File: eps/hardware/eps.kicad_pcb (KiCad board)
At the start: 4 copper layers, 80 x 80 mm, 401 parts, among them J1 USB_C_Receptacle_USB2.0_16P, J10 Conn_02x20_Counter_Clockwise, J11 Conn_01x03, J12 Conn_01x03, J2 Conn_01x02, J3 Conn_01x02, J4 Conn_01x02, J5 Conn_01x02, J6 Conn_01x02, J7 Conn_01x02, J8 Conn_01x02, J9 Conn_02x03_Odd_Even, Q1 NMOS, Q10 IRLML0030, Q11 IRLML0030, Q12 IRLML0030, Q13 IRLML0030, Q14 IRLML0030, Q15 IRLML0030, Q16 IRLML0030, Q17 IRLML0030, Q18 IRLML0030, Q19 IRLML0030, Q2 NMOS, Q20 IRLML0030, Q3 NMOS, Q4 NMOS, Q5 IRLML0030, Q6 IRLML0030, Q7 IRLML0030, Q8 IRLML0030, Q9 IRLML0030, SW1 SW_Push, SW2 SW_SPDT, U1 TPS22810DRV, U10 STM32L496ZGTx, U11 NCS214RSQT2G, U12 74LVC1G07SE-7, U15 NCS214RSQT2G, U16 74LVC1G07SE-7, U19 NCS214RSQT2G, U2 LTC3130-1, U20 74LVC1G07SE-7, U23 NCS214RSQT2G, U24 74LVC1G07SE-7, U27 NCS214RSQT2G, U28 74LVC1G07SE-7, U3 LTC4162-L, U31 NCS214RSQT2G, U32 74LVC1G07SE-7, U35 NCS214RSQT2G, U36 74LVC1G07SE-7, U39 MP28167-A, U4 LTC4162-L, U40 MP28167-A, U41 LTC4415, U42 LTC4415, U5 NCS214RSQT2G, U6 74LVC1G07SE-7, U9 TPS35-Q1, Y1 8MHz, Y2 32KHz

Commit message: start placement
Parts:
- J5, L1, L2, L3, L4, L5, U5, U6, U7, U8: moved to B.Cu
- moved U3 196.0 mm to (232.2, 117.0), turned to 90 degrees
- moved U40 195.3 mm to (234.1, 80.2)
- moved U4 195.2 mm to (221.6, 57.8), turned to -90 degrees
- moved L5 193.3 mm to (234.1, 74.0), turned to 90 degrees
- moved J12 193.3 mm to (235.0, 59.5), turned to 180 degrees
- moved J11 185.4 mm to (230.5, 124.5)
- moved L3 183.7 mm to (224.5, 64.5), turned to -90 degrees
- moved J10 183.1 mm to (201.8, 57.4)
- moved L2 174.7 mm to (223.5, 117.0)
- moved J9 163.2 mm to (221.0, 74.5), turned to -90 degrees
- moved U10 161.0 mm to (203.3, 90.0)
- moved L4 153.4 mm to (236.5, 89.5), turned to 90 degrees
- moved U39 152.8 mm to (234.8, 97.3)
- moved J4 141.3 mm to (236.9, 105.5), turned to 90 degrees
- moved Y2 134.0 mm to (186.0, 84.5), turned to 90 degrees
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
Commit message: schematic fixes
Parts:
- removed J9: Conn_02x03_Odd_Even, Connector_PinHeader_2.54mm:PinHeader_2x03_P2.54mm_Vertical
- added J13: Conn_ARM_JTAG_SWD_10, Connector_PinHeader_1.27mm:PinHeader_2x05_P1.27mm_Vertical_SMD, F.Cu at (218.6, 75.0)
- C1, C10, C100, C101, C102, C103, C104, C105, C106, C107, C108, C11, C110, C111, C112, C113, C114, C115, C116, C117, C118, C119, C12, C120, C122, C123, C124, C125, C126, C127, C128, C129, C13, C130, C131, C132, C133, C134, C135, C136, C137, C138, C139, C14, C140, C141, C142, C143, C144, C15, C16, C17, C18, C19, C2, C20, C21, C22, C23, C24, C25, C26, C27, C28, C29, C3, C30, C31, C32, C33, C34, C35, C36, C37, C38, C39, C4, C40, C41, C42, C43, C44, C45, C46, C47, C49, C5, C51, C52, C53, C54, C55, C56, C57, C58, C59, C6, C60, C61, C62, C63, C64, C65, C66, C67, C68, C69, C7, C70, C71, C72, C73, C74, C75, C76, C77, C78, C79, C8, C80, C81, C82, C83, C84, C85, C86, C87, C88, C89, C9, C90, C91, C92, C93, C94, C95, C96, C97, C98, C99: footprint Capacitor_SMD:C_0603_1608Metric -> Capacitor_SMD:C_0402_1005Metric
- R1, R10, R100, R101, R102, R103, R104, R105, R106, R107, R108, R109, R11, R110, R111, R112, R113, R114, R115, R116, R117, R118, R119, R12, R120, R121, R122, R123, R124, R125, R126, R127, R128, R129, R13, R130, R131, R132, R133, R134, R135, R136, R137, R138, R139, R14, R140, R141, R142, R143, R144, R145, R146, R15, R16, R17, R18, R19, R2, R20, R21, R22, R23, R24, R25, R26, R27, R28, R29, R3, R30, R31, R32, R33, R34, R35, R36, R37, R38, R39, R4, R40, R41, R42, R43, R44, R45, R46, R47, R48, R49, R5, R50, R51, R52, R53, R54, R55, R56, R57, R58, R59, R6, R60, R61, R62, R63, R64, R65, R66, R67, R68, R69, R7, R70, R71, R72, R73, R74, R75, R76, R77, R78, R79, R8, R80, R81, R82, R83, R84, R85, R86, R87, R88, R89, R9, R90, R91, R92, R93, R94, R95, R96, R97, R98, R99: footprint Resistor_SMD:R_0603_1608Metric -> Resistor_SMD:R_0402_1005Metric
- U14, U18, U22, U26, U30, U34, U38: value ~ -> TPS22810DRVT
- U5, U6, U7: moved to F.Cu
- U8: value ~ -> TPS22810DRVT; moved to F.Cu
- moved U7 68.8 mm to (137.9, 120.1)
- moved U5 68.3 mm to (138.4, 124.3)
- moved U8 68.2 mm to (138.4, 112.7), turned to 0 degrees
- moved U6 68.1 mm to (138.5, 116.0)
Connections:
- C13 pad 2: Net-(U3-SW) -> Net-(C13-Pad2)
- C19 pad 2: Net-(U4-SW) -> Net-(C19-Pad2)
- J10 pad 01: (no net) -> GND
- J10 pad 02: (no net) -> /Current Monitors/RAIL_1_VOUT
- J10 pad 03: (no net) -> /Current Monitors/RAIL_2_VOUT
- J10 pad 04: (no net) -> /Current Monitors/RAIL_3_VOUT
- J10 pad 05: (no net) -> /Current Monitors/RAIL_4_VOUT
- J10 pad 06: (no net) -> /Current Monitors/RAIL_5_VOUT
- J10 pad 07: (no net) -> /Current Monitors/RAIL_6_VOUT
- J10 pad 08: (no net) -> /Current Monitors/RAIL_7_VOUT
- J10 pad 09: (no net) -> /Current Monitors/RAIL_8_VOUT
- L2 pad 1: Net-(U3-SW) -> Net-(C13-Pad2)
- L3 pad 1: Net-(U4-SW) -> Net-(C19-Pad2)
- U14 pad 7: (no net) -> unconnected-(U14-GND-Pad7)
- U18 pad 7: (no net) -> unconnected-(U18-GND-Pad7)
- U22 pad 7: (no net) -> unconnected-(U22-GND-Pad7)
- U26 pad 7: (no net) -> unconnected-(U26-GND-Pad7)
- U3 pad 25: Net-(U3-SW) -> Net-(C13-Pad2)
- U3 pad 26: (no net) -> Net-(C13-Pad2)
- U30 pad 7: (no net) -> unconnected-(U30-GND-Pad7)
- U34 pad 7: (no net) -> unconnected-(U34-GND-Pad7)
- U38 pad 7: (no net) -> unconnected-(U38-GND-Pad7)
- U4 pad 25: Net-(U4-SW) -> Net-(C19-Pad2)
- U4 pad 26: (no net) -> Net-(C19-Pad2)
- U8 pad 7: (no net) -> unconnected-(U8-GND-Pad7)

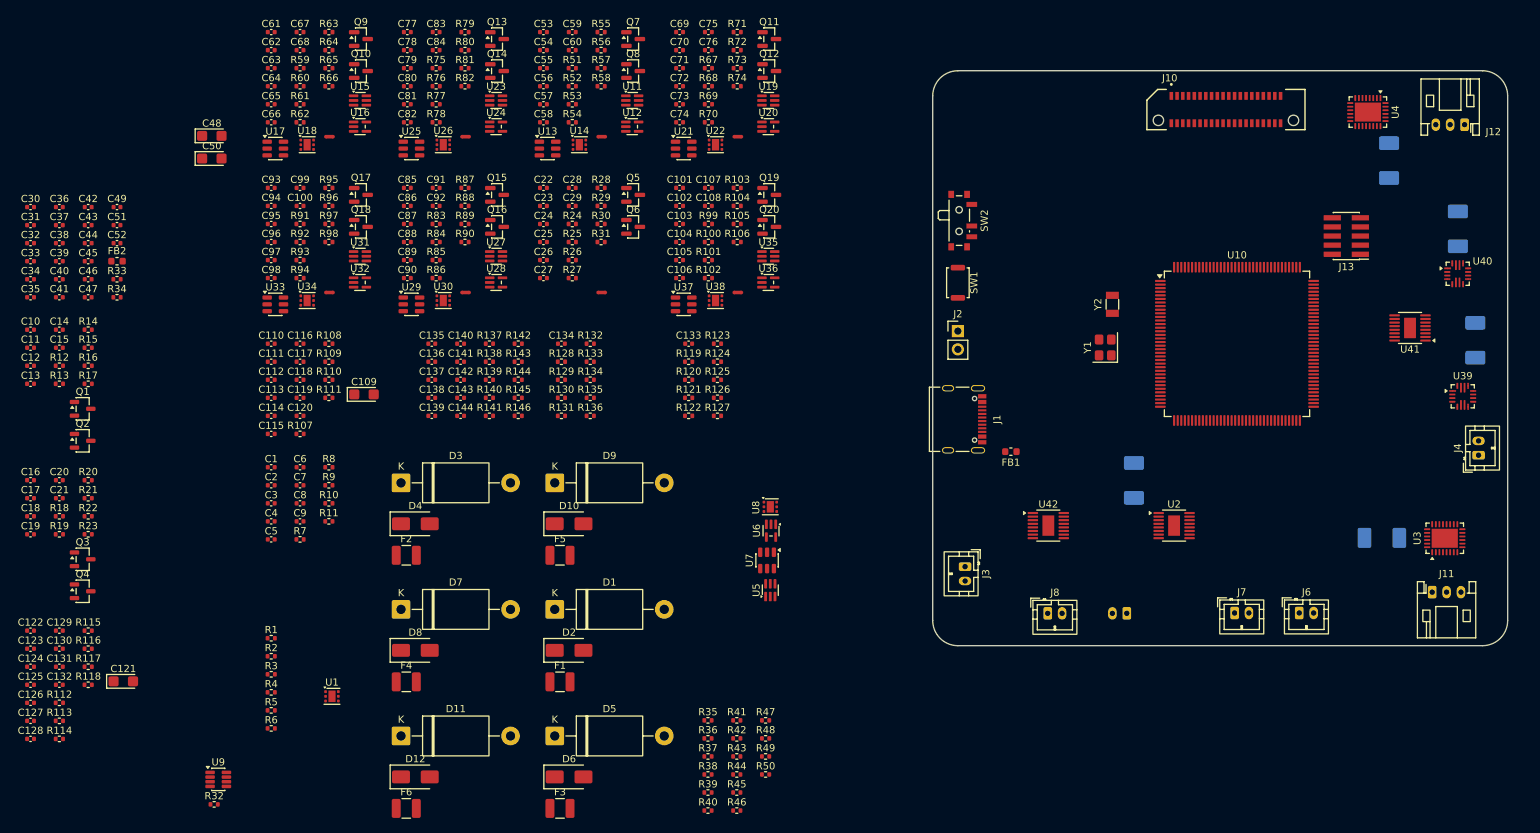
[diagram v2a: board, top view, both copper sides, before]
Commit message: fix all obvious schematic issues
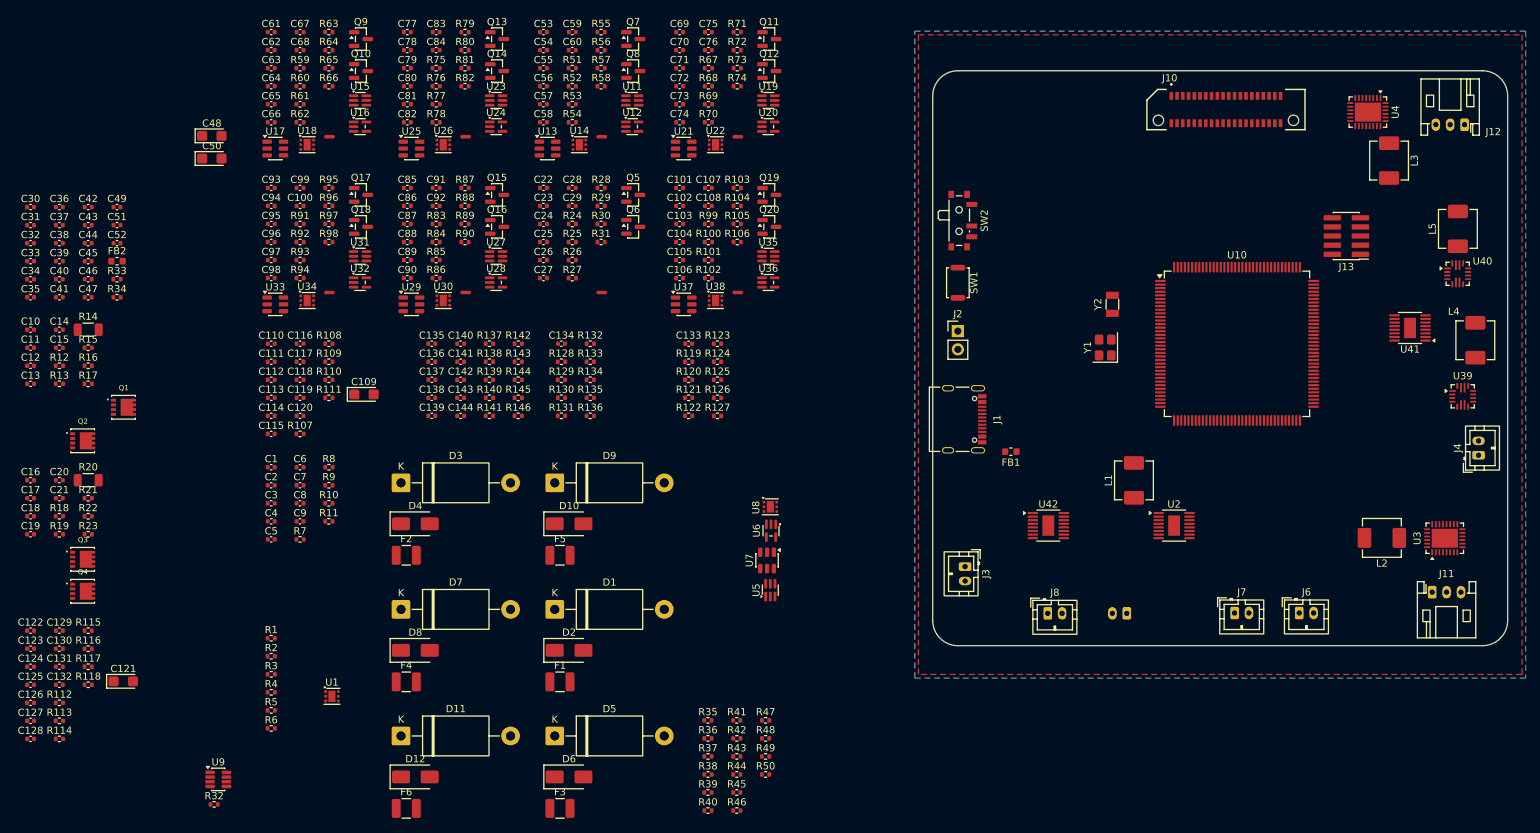
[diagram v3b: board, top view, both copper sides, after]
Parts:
- L1, L2, L3, L4, L5: moved to F.Cu
- Q1, Q2, Q3, Q4: footprint Package_TO_SOT_SMD:SOT-23-3 -> footprints:TRANS_FDMC8327L
- R14, R20: footprint Resistor_SMD:R_0402_1005Metric -> Resistor_SMD:R_1206_3216Metric
- moved Q1 5.69 mm to (48.4, 98.8)
- turned L2 to 180 degrees
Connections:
- L2 pad 2: Net-(Q2-S) -> Net-(U3-CSP)
- L3 pad 2: Net-(Q4-S) -> Net-(Q4-G)_1
- Q1 pad 1: Net-(Q1-D) -> Net-(U3-CLP)
- Q1 pad 2: Net-(Q1-G) -> Net-(U3-CLP)
- Q1 pad 3: /VSYS -> Net-(U3-CLP)
- Q2 pad 2: Net-(Q2-G) -> /Battery Charger/VOUT
- Q2 pad 3: Net-(Q2-S) -> /Battery Charger/VOUT
- Q3 pad 1: Net-(Q3-D) -> Net-(U4-CLP)
- Q3 pad 2: Net-(Q3-G) -> Net-(U4-CLP)
- Q3 pad 3: /VSYS -> Net-(U4-CLP)
- Q4 pad 2: Net-(Q4-G) -> /Battery Charger1/VOUT
- Q4 pad 3: Net-(Q4-S) -> /Battery Charger1/VOUT
- R14 pad 1: Net-(Q1-D) -> Net-(U3-CLP)
- R17 pad 1: Net-(Q2-S) -> Net-(U3-CSP)
- R20 pad 1: Net-(Q3-D) -> Net-(U4-CLP)
- R23 pad 1: Net-(Q4-S) -> Net-(Q4-G)_1
- U3 pad 21: Net-(Q2-S) -> Net-(U3-CSP)
- U3 pad 5: Net-(Q1-D) -> Net-(U3-CLP)
- U4 pad 21: Net-(Q4-S) -> Net-(Q4-G)_1
- U4 pad 5: Net-(Q3-D) -> Net-(U4-CLP)
- U4 pad 6: Net-(Q3-G) -> Net-(U4-INFET)
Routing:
- added copper zone on B.Cu, net GND
- added copper zone on F.Cu, net GND

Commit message: optimize battery charger layout
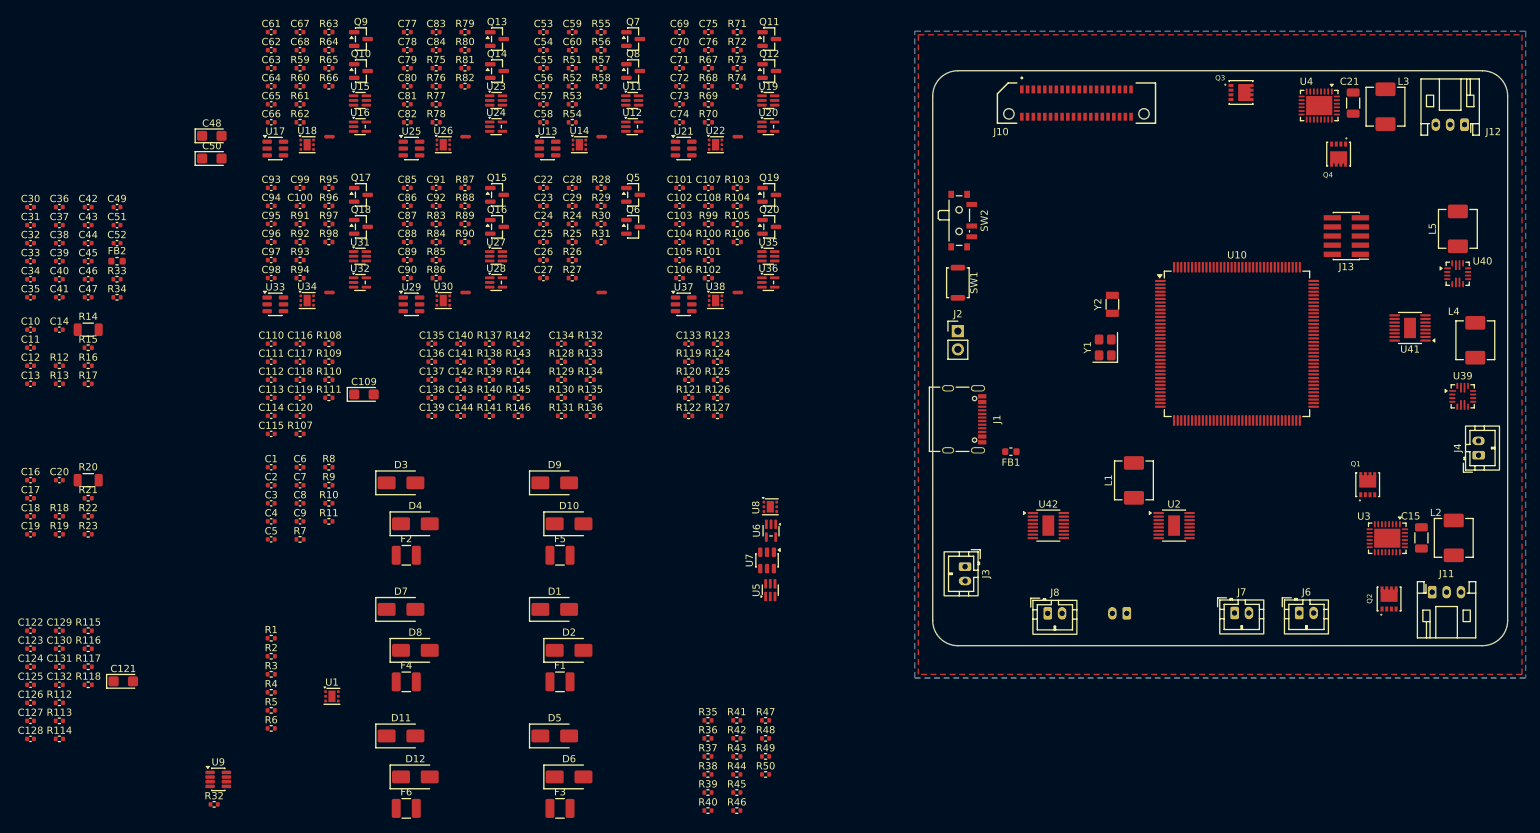
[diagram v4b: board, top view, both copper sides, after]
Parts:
- C15, C21: footprint Capacitor_SMD:C_0402_1005Metric -> Capacitor_SMD:C_1206_3216Metric
- D1, D11, D3, D5, D7, D9: footprint Diode_THT:D_DO-201AE_P15.24mm_Horizontal -> Diode_SMD:D_SMA
- moved C15 191.4 mm to (229.0, 117.0), turned to -90 degrees
- moved C21 188.2 mm to (219.5, 56.5), turned to -90 degrees
- moved Q4 185.0 mm to (217.5, 63.6), turned to -90 degrees
- moved Q2 183.1 mm to (224.5, 125.5), turned to 90 degrees
- moved Q3 173.8 mm to (203.9, 55.0)
- moved Q1 173.5 mm to (221.5, 109.6), turned to 90 degrees
- moved J10 20.8 mm to (181.0, 56.5)
- moved L2 10.0 mm to (233.5, 117.0), turned to -90 degrees
- moved U3 8.00 mm to (224.2, 117.0), turned to -90 degrees
- moved L3 7.52 mm to (224.0, 57.0)
- moved U4 6.83 mm to (214.8, 56.8)

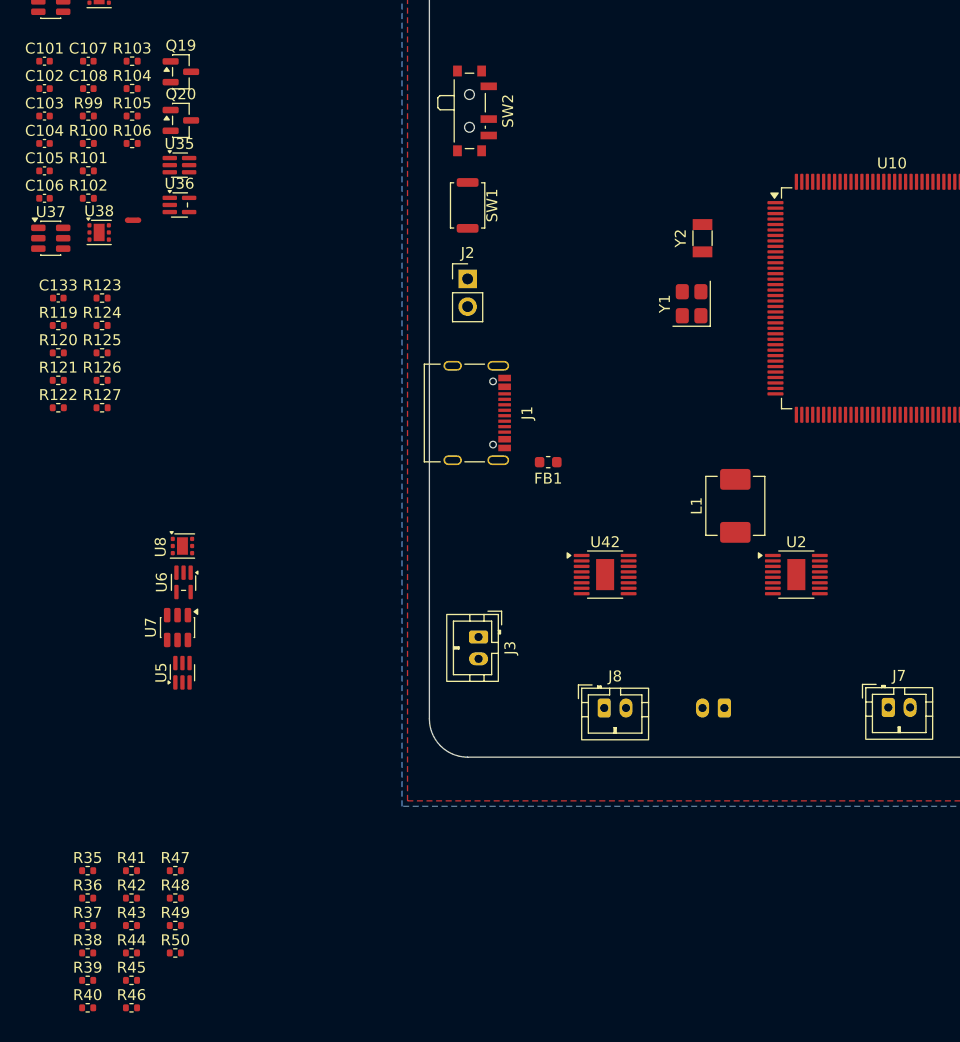
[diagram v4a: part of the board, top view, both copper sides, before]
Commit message: change footprint sizes for current monitoring
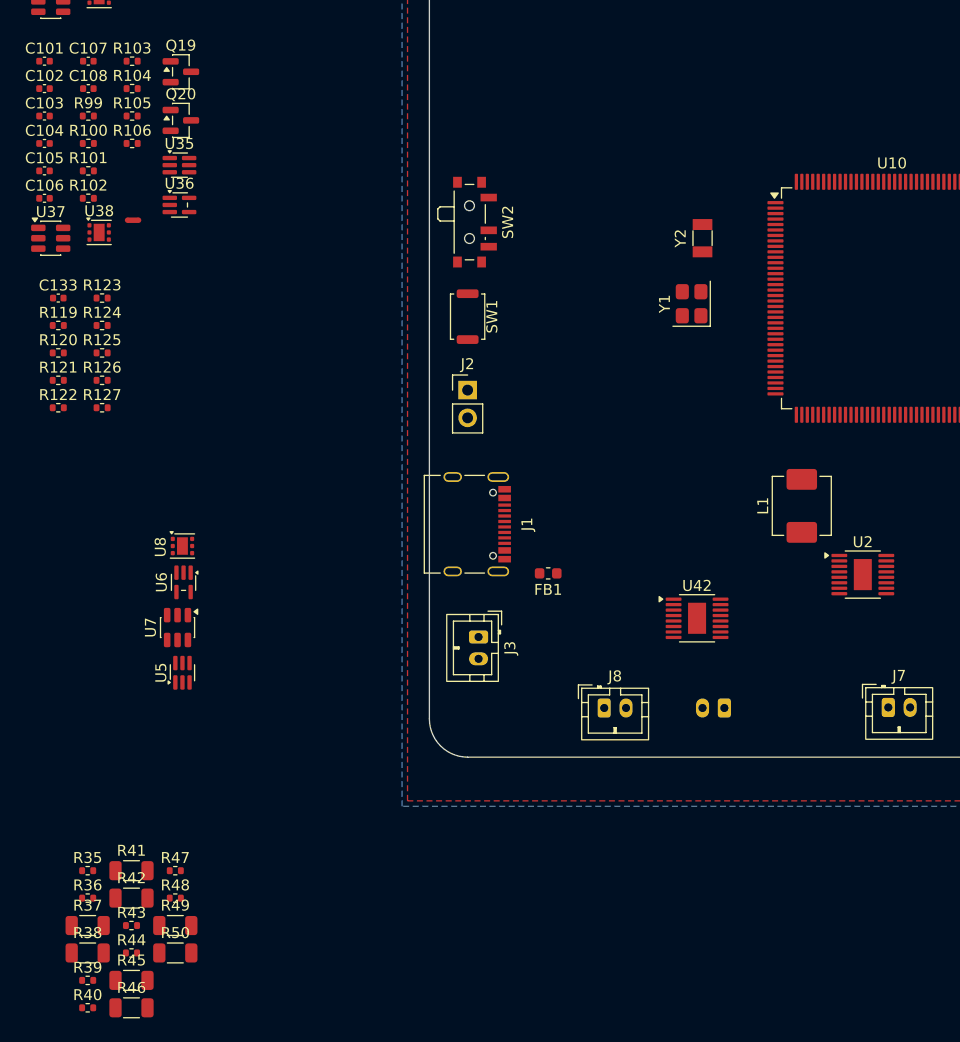
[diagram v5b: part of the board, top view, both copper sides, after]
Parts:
- R37, R38, R41, R42, R45, R46, R49, R50: footprint Resistor_SMD:R_0402_1005Metric -> Resistor_SMD:R_1206_3216Metric
- moved FB1 10.2 mm to (171.9, 115.2)
- moved J1 10.2 mm to (165.4, 110.7)
- moved J2 10.2 mm to (164.5, 98.4)
- moved SW1 10.2 mm to (164.5, 91.7)
- moved SW2 10.2 mm to (165.0, 83.0)
- moved U42 9.32 mm to (185.5, 119.3)
- moved L1 6.09 mm to (195.1, 109.0)
- moved U2 6.08 mm to (200.7, 115.3)
